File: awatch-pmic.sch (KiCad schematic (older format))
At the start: 19 parts, among them J301 Conn_01x02, U301 MAX14690A

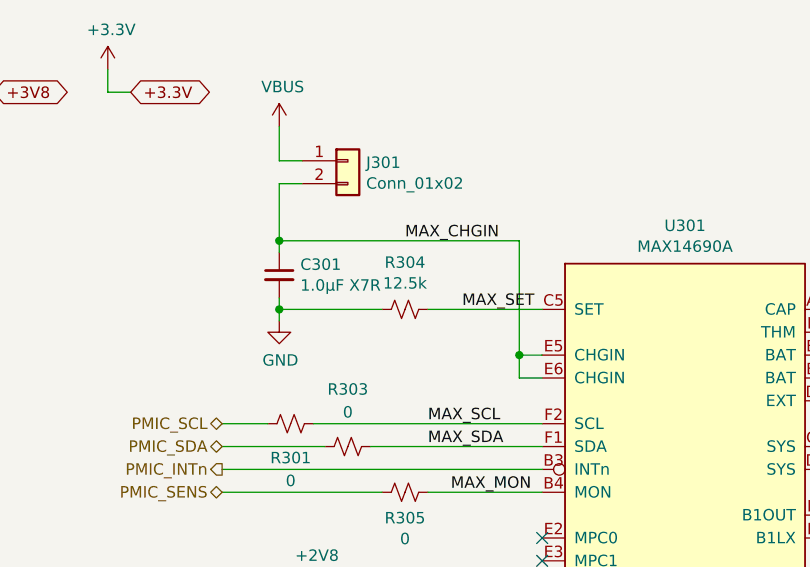
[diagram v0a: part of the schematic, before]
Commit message: BOM fully populated
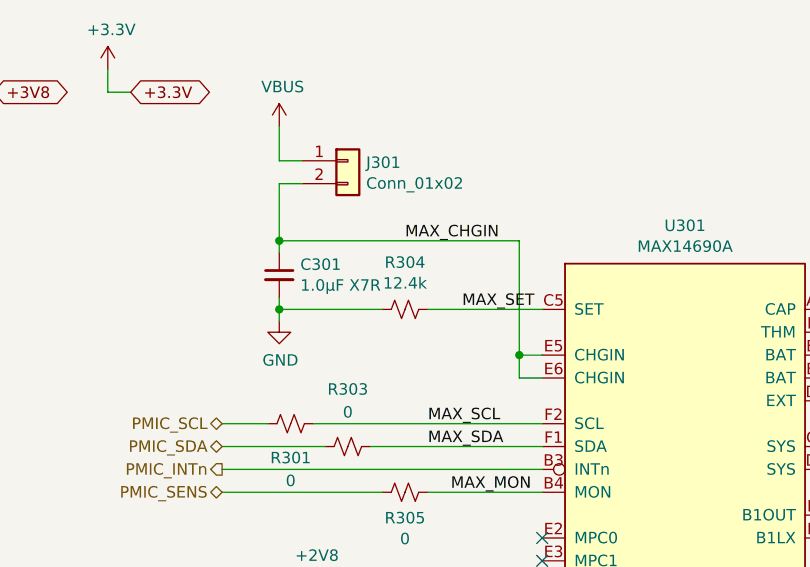
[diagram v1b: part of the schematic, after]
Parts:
- J301: DigiKey PN (none) -> S1011EC-02-ND, S9341-ND
- L301: DigiKey PN (none) -> 445-6385-1-ND
- R301, R303, R305, R306: DigiKey PN (none) -> MCT0603-0.0-ZZCT-ND
- R302, R307: DigiKey PN (none) -> MCT0603-10.0K-CFCT-ND
- R304: value 12.5k -> 12.4k; DigiKey PN (none) -> RNCP0603FTD12K4CT-ND
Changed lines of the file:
@@
 F 2 "Resistor_SMD:R_0603_1608Metric" H 3600 3600 50  0001 C CNN
 F 3 "~" H 3600 3600 50  0001 C CNN
+F 4 "MCT0603-10.0K-CFCT-ND" H 0   0   50  0001 C CNN "DigiKey PN"
 	1    3600 3600
 	-1   0    0    1
@@
 P 4000 2200
 F 0 "R304" V 3795 2200 50  0000 C CNN
-F 1 "12.5k" V 3886 2200 50  0000 C CNN
+F 1 "12.4k" V 3886 2200 50  0000 C CNN
 F 2 "Resistor_SMD:R_0603_1608Metric" H 4000 2200 50  0001 C CNN
 F 3 "~" H 4000 2200 50  0001 C CNN
+F 4 "RNCP0603FTD12K4CT-ND" H 0   0   50  0001 C CNN "DigiKey PN"
 	1    4000 2200
 	0    1    1    0
@@
 F 2 "Resistor_SMD:R_0603_1608Metric" H 6650 2300 50  0001 C CNN
 F 3 "~" H 6650 2300 50  0001 C CNN
+F 4 "MCT0603-10.0K-CFCT-ND" H 0   0   50  0001 C CNN "DigiKey PN"
 	1    6650 2300
 	0    1    1    0
@@
 F 2 "Inductor_SMD:L_0603_1608Metric" H 6100 3500 50  0001 C CNN
 F 3 "~" H 6100 3500 50  0001 C CNN
+F 4 "445-6385-1-ND" H 0   0   50  0001 C CNN "DigiKey PN"
 	1    6100 3500
 	0    -1   -1   0
@@
 F 2 "Resistor_SMD:R_0603_1608Metric" H 4100 3800 50  0001 C CNN
 F 3 "~" H 4100 3800 50  0001 C CNN
+F 4 "MCT0603-0.0-ZZCT-ND" H 0   0   50  0001 C CNN "DigiKey PN"
 	1    4100 3800
 	0    1    1    0
@@
 F 2 "Resistor_SMD:R_0603_1608Metric" H 3500 2700 50  0001 C CNN
 F 3 "~" H 3500 2700 50  0001 C CNN
+F 4 "MCT0603-0.0-ZZCT-ND" H 0   0   50  0001 C CNN "DigiKey PN"
 	1    3500 2700
 	0    1    1    0
@@
 F 2 "Resistor_SMD:R_0603_1608Metric" H 3750 2800 50  0001 C CNN
 F 3 "~" H 3750 2800 50  0001 C CNN
+F 4 "MCT0603-0.0-ZZCT-ND" H 0   0   50  0001 C CNN "DigiKey PN"
 	1    3750 2800
 	0    1    1    0
@@
 F 2 "Resistor_SMD:R_0603_1608Metric" H 4000 3000 50  0001 C CNN
 F 3 "~" H 4000 3000 50  0001 C CNN
+F 4 "MCT0603-0.0-ZZCT-ND" H 0   0   50  0001 C CNN "DigiKey PN"
 	1    4000 3000
 	0    1    1    0
@@
 F 2 "Connector_PinHeader_2.54mm:PinHeader_1x02_P2.54mm_Vertical" H 3750 1550 50  0001 C CNN
 F 3 "~" H 3750 1550 50  0001 C CNN
+F 4 "S1011EC-02-ND, S9341-ND" H 0   0   50  0001 C CNN "DigiKey PN"
 	1    3750 1550
 	1    0    0    -1
